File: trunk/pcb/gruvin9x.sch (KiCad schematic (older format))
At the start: 153 parts, among them K1 CONN_3, K2 CONN_3, P1 CONN_5X2, P10 CONN_1, P11 CONN_1, P12 CONN_1, P13 CONN_8, P14 CONN_2, P15 CONN_1, P2 CONN_5, P3 CONN_6, P4 CONN_9, P5 CONN_9, P6 CONN_6, P7 CONN_12, P8 CONN_30, P9 CONN_1, Q1 2SC9014, Q2 NPN, Q3 NPN, SW1 SW_PUSH, SW2 SW_PUSH, SW3 SW_PUSH, SW4 SW_PUSH, SW5 SW_PUSH, SW6 SW_PUSH, U1 78L05, U2 4066, U3 LN-6206-30, X1 16MHz

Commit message: The big change to gruvin9x naming instead of er9x -- it finally got too confusing, going between versions, checking code diffs, etc. NO FUNCTIONAL CHANGES this revision.
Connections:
- wire segments 582 -> 493
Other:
- note added: "(Pseudo)\nRS-232 TRX"
- note removed: "RS-232 TRX"

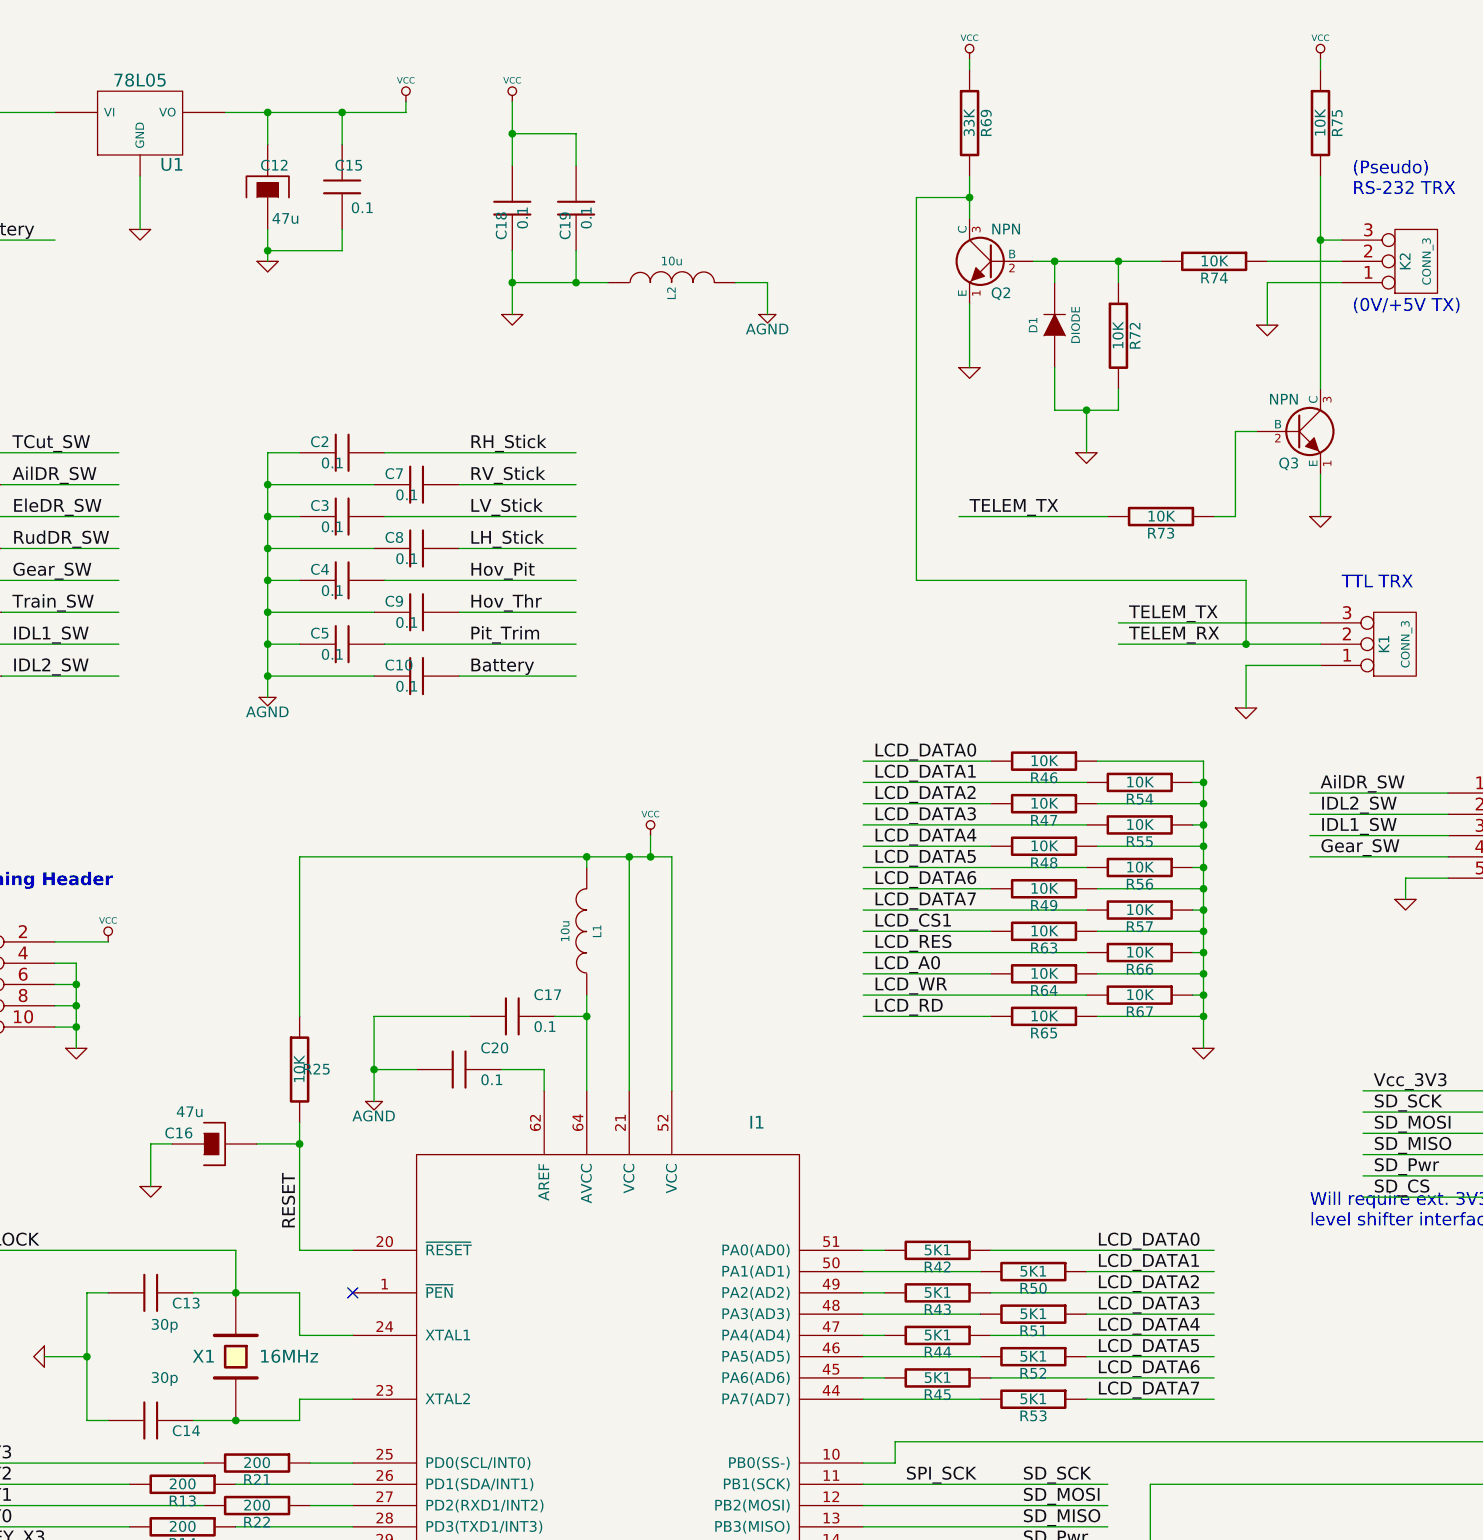
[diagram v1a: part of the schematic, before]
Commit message: PCB production output files generated
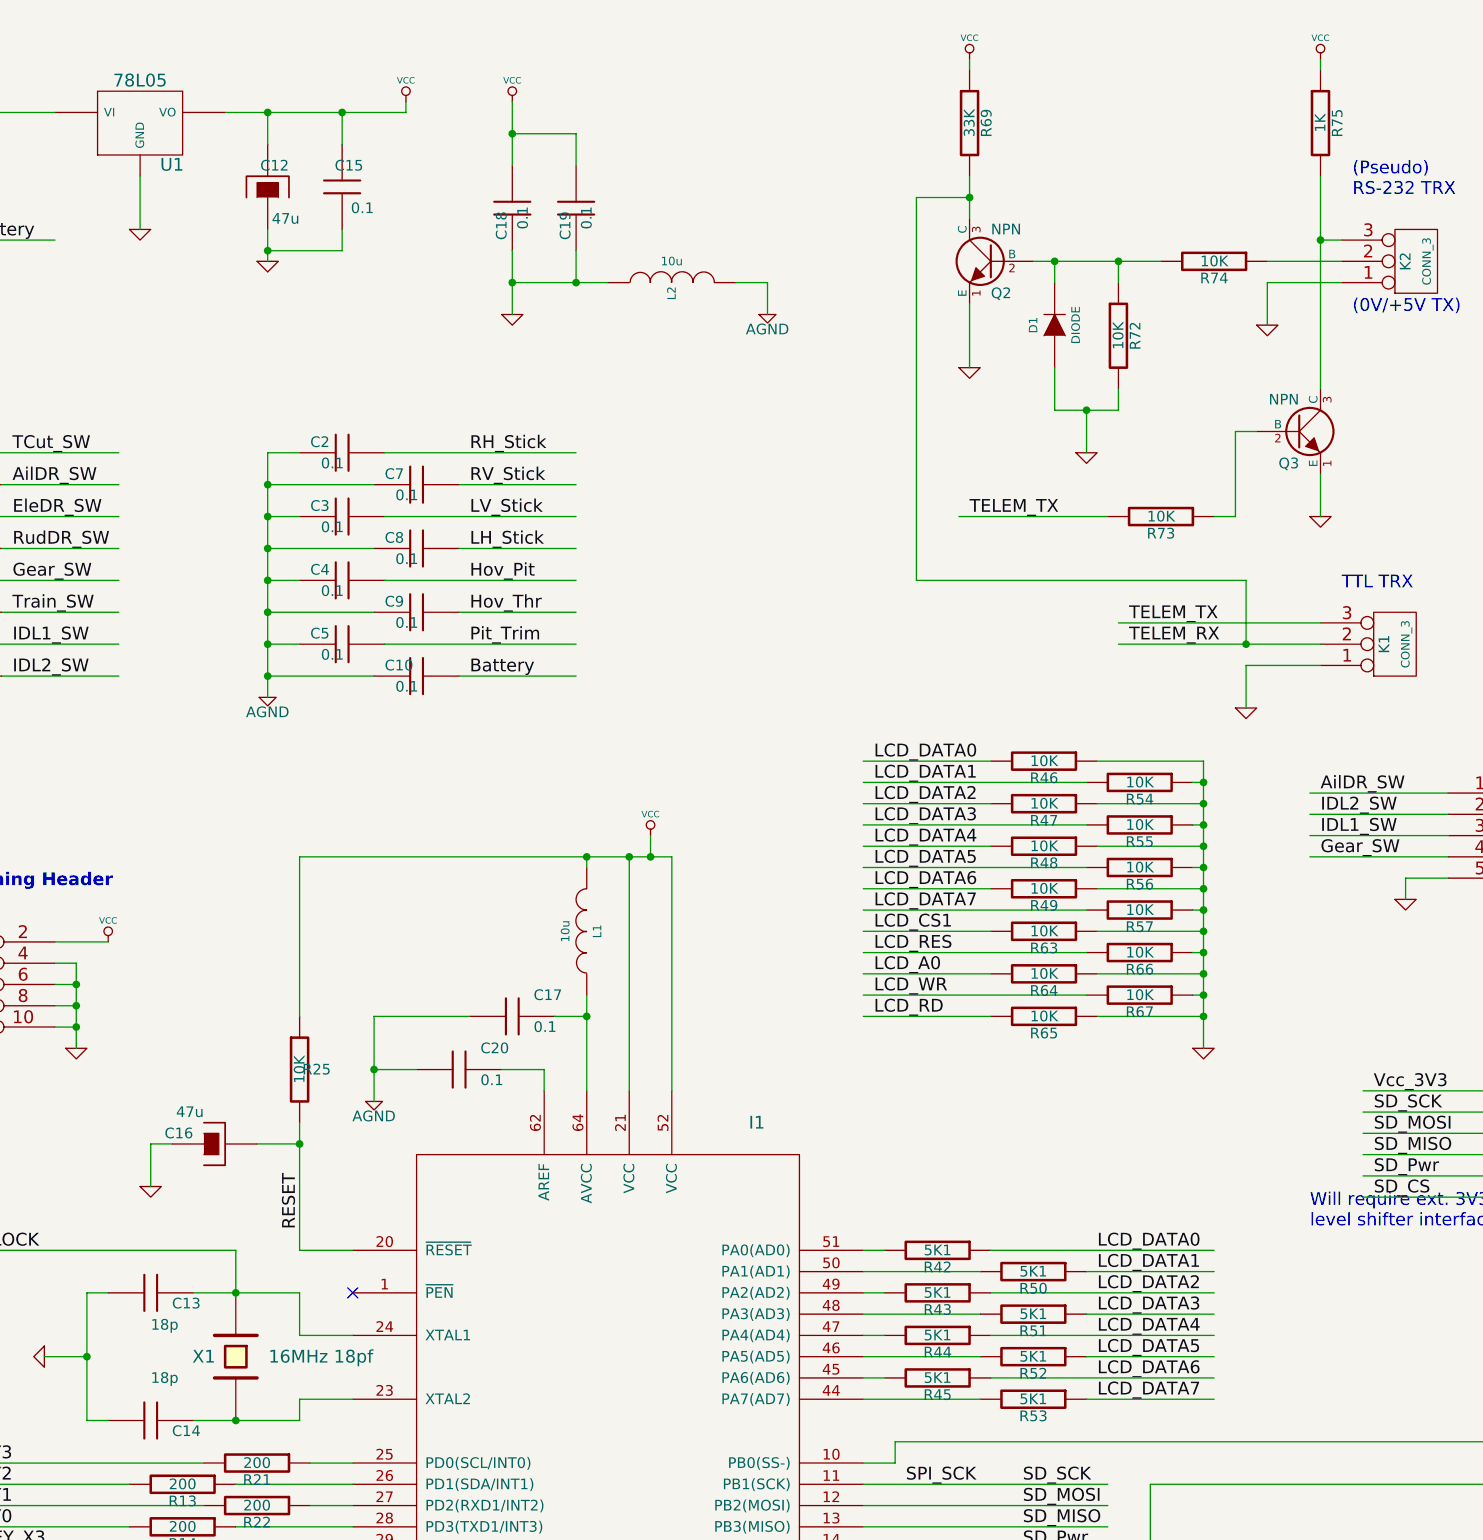
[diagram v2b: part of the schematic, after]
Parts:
- C13, C14: value 30p -> 18p
- R75: value 10K -> 1K
- X1: value 16MHz -> 16MHz 18pf
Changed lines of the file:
@@
-EESchema Schematic File Version 2  date 2/12/2010 5:54:13 p.m.
+EESchema Schematic File Version 2  date 9/12/2010 1:22:50 p.m.
 LIBS:conn_5
 LIBS:atmega64
@@
 Sheet 1 1
 Title "Main Controller PCB (Stock)"
-Date "2 dec 2010"
+Date "9 dec 2010"
 Rev "2.11"
 Comp "gruvin9x"
@@
 P 8200 1000
 F 0 "R75" V 8280 1000 50  0000 C CNN
-F 1 "10K" V 8200 1000 50  0000 C CNN
+F 1 "1K" V 8200 1000 50  0000 C CNN
 	1    8200 1000
 	1    0    0    -1
@@
 P 2700 7100
 F 0 "C14" V 2750 7200 50  0000 L CNN
-F 1 "30p" V 2500 7100 50  0000 L CNN
+F 1 "18p" V 2500 7100 50  0000 L CNN
 	1    2700 7100
 	0    1    1    0
@@
 P 2700 6500
 F 0 "C13" V 2750 6600 50  0000 L CNN
-F 1 "30p" V 2850 6500 50  0000 L CNN
+F 1 "18p" V 2850 6500 50  0000 L CNN
 	1    2700 6500
 	0    1    1    0
@@
 P 3100 6800
 F 0 "X1" V 3100 6650 60  0000 C CNN
-F 1 "16MHz" V 3100 7050 60  0000 C CNN
+F 1 "16MHz 18pf" V 3100 7200 60  0000 C CNN
 	1    3100 6800
 	0    1    1    0

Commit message: Schematic v2.12 changed to improve RS-232 output (now PNP). PCB v2.12 changed to match.
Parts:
- added R76: 10K, symbol R
- Q3: value NPN -> PNP; symbol NPN -> PNP
- R69: value 33K -> 10K
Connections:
- wire segments 493 -> 498
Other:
- moved on the sheet: D1, K1, K2, Q2, R69, R72, R73, R74, R75

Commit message: Updated and uploaded v2.13 circuit schematic, board and production files
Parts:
- added P16, P17: CONN_1, symbol CONN_1
- added R77, R78: 0, symbol R
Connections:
- net labels added: J1, J2, Spare1
- net labels removed: Spare3
- wire segments 498 -> 510
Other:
- moved on the sheet: R14, R22

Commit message: Schematic/PCB rev2.14 finalised for prototype production.
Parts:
- removed Q1: 2SC9014, SOT23EBD, symbol NPN
- removed Q2: NPN, symbol NPN
- removed Q3: PNP, symbol PNP
- added Q1, Q2: BC847C, SOT23-BCE, symbol BC847C
- added Q3: BC857C, SOT23-BCE, symbol BC857C
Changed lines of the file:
@@
-EESchema Schematic File Version 2  date 10/12/2010 1:16:18 p.m.
+EESchema Schematic File Version 2  date 12/12/2010 12:18:23 p.m.
 LIBS:conn_5
 LIBS:atmega64
@@
 LIBS:contrib
 LIBS:valves
+LIBS:trans-sot23
 LIBS:gruvin9x-cache
 EELAYER 24  0
@@
 Sheet 1 1
 Title "Main Controller PCB (Stock)"
-Date "9 dec 2010"
-Rev "2.13"
+Date "11 dec 2010"
+Rev "2.14"
 Comp "gruvin9x"
 Comment1 ""
@@
 Comment4 ""
 $EndDescr
+$Comp
+L BC857C Q3
+U 1 1 4D04001D
+P 7650 1050
+F 0 "Q3" H 7850 950 50  0000 C CNN
+F 1 "BC857C" H 7950 1200 50  0000 C CNN
+F 2 "SOT23-BCE" H 7840 1050 30  0001 C CNN
+	1    7650 1050
+	1    0    0    -1
+$EndComp
+$Comp
+L BC847C Q2
+U 1 1 4D03FFF9
+P 6550 2050
+F 0 "Q2" H 6450 1900 50  0000 C CNN
+F 1 "BC847C" H 6400 2250 50  0000 C CNN
+F 2 "SOT23-BCE" H 6740 2050 30  0001 C CNN
+	1    6550 2050
+	-1   0    0    -1
+$EndComp
+$Comp
+L BC847C Q1
+U 1 1 4D03FF83
+P 12150 7700
+F 0 "Q1" H 12000 7600 50  0000 C CNN
+F 1 "BC847C" H 11950 7900 50  0000 C CNN
+F 2 "SOT23-BCE" H 12340 7700 30  0001 C CNN
+	1    12150 7700
+	-1   0    0    -1
+$EndComp
 Text Label 1250 6750 0    60   ~ 0
 J2
@@
 	1    7050 1550
 	1    0    0    -1
-$EndComp
-$Comp
-L PNP Q3
-U 1 1 4CF47EAA
-P 7650 1050
-F 0 "Q3" H 7650 900 50  0000 R CNN
-F 1 "PNP" H 7650 1200 50  0000 R CNN
-	1    7650 1050
-	1    0    0    1
 $EndComp
 Text Label 7200 3300 0    60   ~ 0
@@
 	1    0    0    -1
 $EndComp
-$Comp
-L NPN Q2
-U 1 1 4CEE079E
-P 6550 2050
-F 0 "Q2" H 6550 1900 50  0000 R CNN
-F 1 "NPN" H 6550 2200 50  0000 R CNN
-	1    6550 2050
-	-1   0    0    -1
-$EndComp
 Text Label 7200 3400 0    60   ~ 0
 TELEM_RX
@@
 	0    1    1    0
 $EndComp
-$Comp
-L NPN Q1
-U 1 1 4CE75FF5
-P 12150 7700
-F 0 "Q1" H 12150 7550 50  0000 R CNN
-F 1 "2SC9014" H 12150 7850 50  0000 R CNN
-F 2 "SOT23EBD" H 12100 7500 60  0001 C CNN
-	1    12150 7700
-	-1   0    0    -1
-$EndComp
 Text Label 13600 6950 0    60   ~ 0

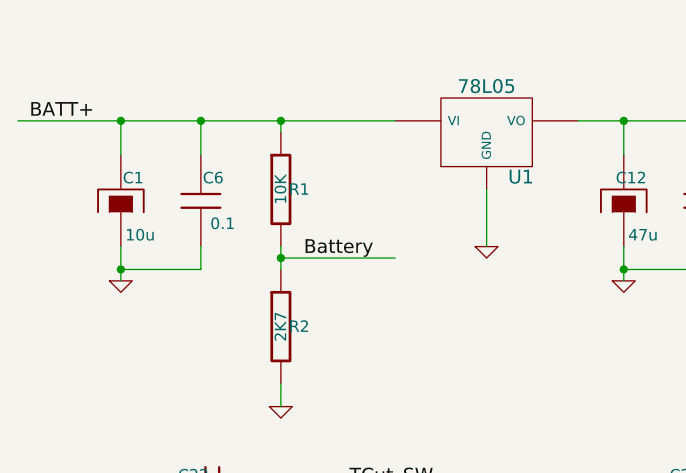
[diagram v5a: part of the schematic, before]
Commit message: Added Turnigy 9X V2 backup firmware to allow restoring of original V2 factory firmware. (This firmware as supplied by http://HobbyKing.com)
Corrected error in all circuit schematic versiosn -- R1 is a 5K1, not a 10K.
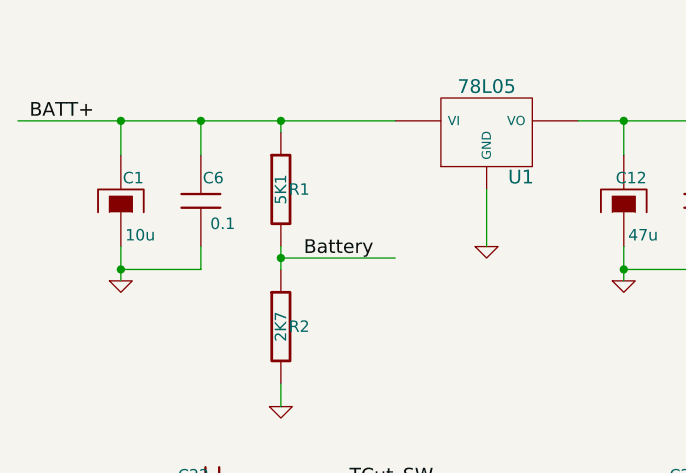
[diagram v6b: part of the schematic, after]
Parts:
- R1: value 10K -> 5K1
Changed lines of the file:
@@
-EESchema Schematic File Version 2  date 12/12/2010 12:18:23 p.m.
+EESchema Schematic File Version 2  date 14/12/2010 1:53:32 p.m.
 LIBS:conn_5
 LIBS:atmega64
@@
 Sheet 1 1
 Title "Main Controller PCB (Stock)"
-Date "11 dec 2010"
+Date "14 dec 2010"
 Rev "2.14"
 Comp "gruvin9x"
@@
 P 1750 1250
 F 0 "R1" H 1830 1250 50  0000 C CNN
-F 1 "10K" V 1750 1250 50  0000 C CNN
+F 1 "5K1" V 1750 1250 50  0000 C CNN
 	1    1750 1250
 	1    0    0    -1

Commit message: Updates to PCB rev2.14 BOM files after discovering problems with parts from first prototype order, as follows:
+ SMD30 LCD FPC connector FAR too brittle. Replaced with different brand (yet to 
  determine new brand's final suitability.)

+ Push button switches wrong length. Should be 9.5mm height, not 13mm. Corrected.

+ All resistors mistakenly ordered 0608 metric, instead of 0608 imperial. Corrected.

+ 18p capacitors (for Xtal) also 0201 (0608 metric) instead of 0608. Corrected.

+ Male (plug) parts of JST sockets are not included with socket part numbers. Added
  those, including enough crimp terminals to populate.

+ Both regulators (5V and 3V3) missing from BOM altogether. Added.

Minor grounding vias correction added to V3 PCB file (lower left corner - not GND net.)
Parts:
- added Q?: BC549, SOT23EBD, symbol NPN
- added R?: 330, symbol R
- added R?: 150K, symbol R
- added R?: 4K7, symbol R
- I1: value ATMEGA128A -> ATmega2561
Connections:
- wire segments 510 -> 519
